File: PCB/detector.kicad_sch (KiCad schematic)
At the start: 13 parts, among them J1 Audio In, J3 Through, U2 TL072, U4 LM393

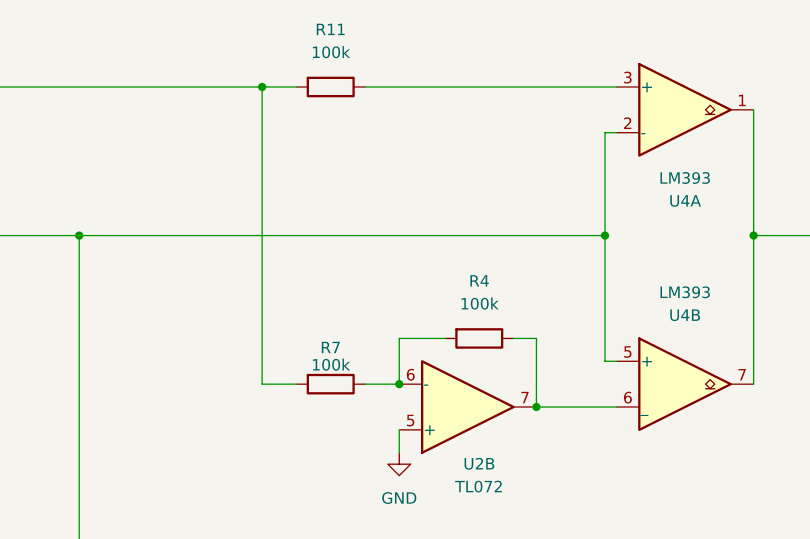
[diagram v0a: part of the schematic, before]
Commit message: :wrench: Adjust the voltage dividers for Clip CV
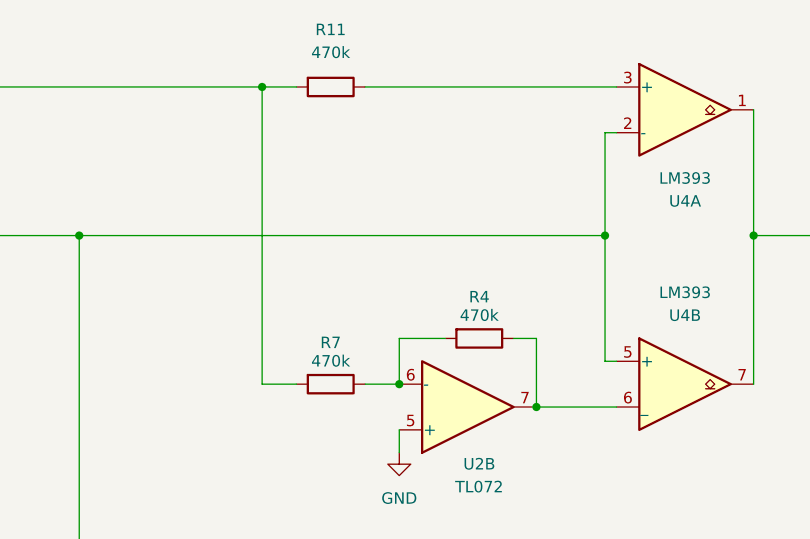
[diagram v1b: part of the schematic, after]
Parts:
- R11, R4, R7: value 100k -> 470k
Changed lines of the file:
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@@
       (effects (font (size 1.27 1.27)))
     )
-    (property "Value" "100k" (at 151.13 48.26 90)
+    (property "Value" "470k" (at 151.13 48.26 90)
       (effects (font (size 1.27 1.27)))
     )
@@
   (symbol (lib_id "Device:R") (at 151.13 85.09 270) (unit 1)
     (in_bom yes) (on_board yes) (dnp no) (fields_autoplaced)
-    (property "Reference" "R7" (at 151.13 81.0641 90)
-      (effects (font (size 1.27 1.27)))
-    )
-    (property "Value" "100k" (at 151.13 82.9851 90)
+    (property "Reference" "R7" (at 151.13 80.494 90)
+      (effects (font (size 1.27 1.27)))
+    )
+    (property "Value" "470k" (at 151.13 82.542 90)
       (effects (font (size 1.27 1.27)))
     )
@@
   (symbol (lib_id "Device:R") (at 167.64 80.01 270) (unit 1)
     (in_bom yes) (on_board yes) (dnp no) (fields_autoplaced)
-    (property "Reference" "R4" (at 167.64 73.66 90)
-      (effects (font (size 1.27 1.27)))
-    )
-    (property "Value" "100k" (at 167.64 76.2 90)
-      (effects (font (size 1.27 1.27)))
-    )
+    (property "Reference" "R4" (at 167.64 75.414 90)
+      (effects (font (size 1.27 1.27)))
+    )
+    (property "Value" "470k" (at 167.64 77.462 90)
+      (effects (font (size 1.27 1.27)))
+    )
